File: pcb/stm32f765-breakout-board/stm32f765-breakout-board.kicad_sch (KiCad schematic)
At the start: 0 parts

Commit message: Updated titleblock on f765 breakout pcb
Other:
- company: (none) -> Pranav Chandra N. V.
- title: (none) -> STM32F765VIT6 Breakout Board
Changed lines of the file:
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@@
 	(generator_version "9.0")
 	(paper "A4")
+	(title_block
+		(title "STM32F765VIT6 Breakout Board")
+		(date "2026-04-17")
+		(rev "v5")
+		(company "Pranav Chandra N. V.")
+		(comment 1 "v4: Manufactured PCB")
+		(comment 2 "v5: Updated title blocks on all pages")
+	)
 	(sheet
 		(at 123.825 81.915)

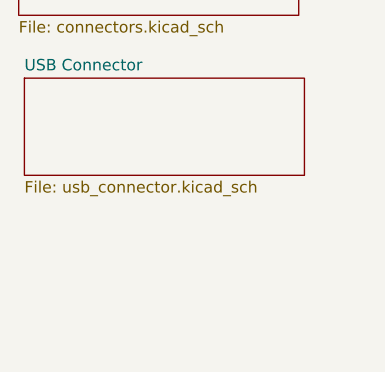
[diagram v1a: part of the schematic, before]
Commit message: Added on board LED to PCB and blinky for board
v6 of the PCB now has an in built on board LED to PE02, to allow for
faster debugging.

The first assembled prototype finally worked, and a blinky sketch was
flashed to test. Relevant code has been added to firmware.
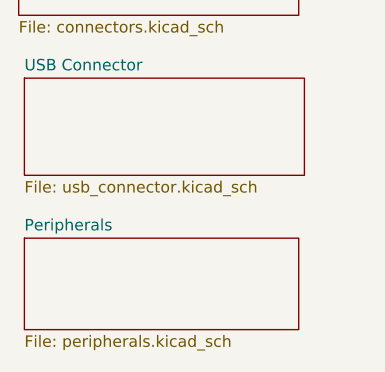
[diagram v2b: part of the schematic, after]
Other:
- added sheet Peripherals (peripherals.kicad_sch)
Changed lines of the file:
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@@
+	)
+	(sheet
+		(at 124.46 134.62)
+		(size 30.48 10.16)
+		(exclude_from_sim no)
+		(in_bom yes)
+		(on_board yes)
+		(dnp no)
+		(fields_autoplaced yes)
+		(stroke
+			(width 0.1524)
+			(type solid)
+		)
+		(fill
+			(color 0 0 0 0.0000)
+		)
+		(property "Sheetname" "Peripherals"
+			(at 124.46 133.9084 0)
+			(effects
+				(font
+					(size 1.27 1.27)
+				)
+				(justify left bottom)
+			)
+		)
+		(property "Sheetfile" "peripherals.kicad_sch"
+			(at 124.46 145.3646 0)
+			(effects
+				(font
+					(size 1.27 1.27)
+				)
+				(justify left top)
+			)
+		)
+		(instances
+			(project "stm32f765-breakout-board"
+				(path "/256bcd66-93a7-4ec7-b605-dbc945027d42"
+					(page "6")
+				)
+			)
+		)
 	)
 	(sheet
@@
 	)
 	(embedded_fonts no)
+	(embedded_files
+		(file
+			(name "main_template.kicad_wks")
+			(type worksheet)
+			(data |KLUv/WCHCq0VAKYeYSEA1TZqxSYpSnAbvBZXs5wAOGKZeWHW4zrjCpNZ+v8JBRNXAFAAWwCj/tcf
+				qX+jwXtSz1izvRHzmSsWLKWmbz7EoJuxWLAU9TvC5YfuEwCAAOn5W04KmzDT1o/DixHJybd+b998
+				NQRAoHBRSqs6q2eNy30/BECg7IAwoQfiDiGfdYa6rV5qcqKTf+j+93ZWtvq0otAGM37vknfvm7cG
+				X/Tpc+qAWvz8io/f7+Y9zB69PZ/88x1HDVbHLoyiHuZ7UdP6pNR/e19Ok9/Ryw/eHd64dcb3Jb0J
+				RZtkkxHmQlF/btXNolE+l3JdkzsoZTk2aUSycRTNgllkis1BGlgKow6OuEpaly0wWoXjNtLAE/e9
+				xd5btO/nC7oog7/0cGx1momq9fl936QVIBCBgnVRC3Ed5qRsddl6qBaramVVrKKHOivaRTSIKHvk
+				qBWzXiLZBCJRIBpdNuk0rcFdV0VZkCyiPTYGZoBY9B57oXpFUJNqj27rxMddpSH2v3fDCQwlQbhN
+				/gGAiaABSYYUDYkkSQoZ5oBEpOaoOozVNJ4pks/fiE0ZYQwgJSGD6wSyrriywopiggHII25zAoVs
+				XFbx0JeoRBjENn6ZPNfwMAiB7v1Jao+tsR3fbItsc6cfa22SwPMnbyvPHcsCfNiQbTqtxVlLMuyT
+				Q1CBRmZJpUc4pQ9d6hFpkGKo5kDuOq5adyoQnBVWLyX04o7iaQH+xWIuAKszPgbRT71kepu0ahHJ
+				5rySzSN2G6MZTKGEeFgCpeAjEDEylaH6xVARFuhl3ozP4iGJaeTxSXanUpT5cOL42wR3pphhO//Z
+				40AJWebRI0cgaGFkJ8ZBXrR3eNWHXAgAXP2GzD6THl2sihfFfNSB65xJb3veSYfQvsmqkQcUuzti
+				bryslIAVCnt4R7z3TYeQjY9eBQ==|
+			)
+			(checksum "2F156D714875550A13BB058F8E490E47")
+		)
+	)
 )
